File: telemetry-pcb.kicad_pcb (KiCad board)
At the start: 4 copper layers, 105 x 70 mm, 79 parts, among them CN1 12V, CN2 UART, CN3 RS232, CN5 THERMO1, CN6 THERMO2, CN8 GPS, IC1 MAX3232CPWR, IC2 MAX31855K, IC3 MAX31855K, IC4 MCP2515-xSO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

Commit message: routing update
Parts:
- moved R9 13.2 mm to (185.4, 99.8), turned to 90 degrees
- moved R7 9.97 mm to (186.5, 73.2), turned to -90 degrees
- moved T6 3.19 mm to (170.7, 79.1)
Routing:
- net /SPI Peripherals/CANL: track 13.1 -> 43.2 mm
- net /SPI Peripherals/CANH: track 62.5 -> 49.6 mm, vias 1 -> 0
- net Net-(S2-A): track 50.3 -> 38.8 mm, vias 3 -> 2
- net /MO: track 65.8 -> 71.3 mm, vias 1 -> 0
- net Net-(J3-Pin_2): track 5.96 -> 9.17 mm
- net /Serial Peripherals/TX_232: track 51.7 -> 53.7 mm
- net +3V3: track 52.8 -> 50.9 mm
- net /MI: track 82.0 -> 83.9 mm, vias 1 -> 2
- net /Serial Peripherals/RX_232: track 49.5 -> 51.0 mm
- net Net-(J2-Pin_5): track 70.0 -> 68.6 mm
- net /A1: track 83.4 -> 84.8 mm, vias 2 -> 1
- net /A0: track 71.7 -> 73.0 mm
- net /SCK: track 92.2 -> 93.5 mm
- net /SDA: track 131.5 -> 132.7 mm
- net Net-(IC1-ROUT1): track 79.8 -> 80.8 mm
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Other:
- outline, holes or cut-outs redrawn

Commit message: a
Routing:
- net GND: track 66.1 -> 67.8 mm, vias 29 -> 30
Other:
- outline, holes or cut-outs redrawn
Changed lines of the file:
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@@
 	)
 	(gr_line
-		(start 94.8944 54.682)
+		(start 94.9706 54.682)
 		(end 189.8396 54.686029)
 		(stroke
@@
 	)
 	(gr_arc
-		(start 194.945312 119.679866)
-		(mid 193.505286 123.184076)
-		(end 190.0174 124.6632)
+		(start 194.945511 119.679866)
+		(mid 193.505427 123.184216)
+		(end 190.017401 124.663399)
 		(stroke
 			(width 0.1)
@@
 	)
 	(gr_arc
-		(start 90 59.682)
-		(mid 91.464466 56.146466)
-		(end 95 54.682)
+		(start 89.999914 59.682)
+		(mid 91.454026 56.156815)
+		(end 94.9706 54.682)
 		(stroke
 			(width 0.1)
@@
 	)
 	(segment
+		(start 160.3248 100.4062)
+		(end 161.18 100.4062)
+		(width 0.25)
+		(layer "F.Cu")
+		(net 1)
+	)
+	(segment
 		(start 114.189 113.093)
 		(end 114.25 113.032)
@@
 	)
 	(segment
+		(start 161.18 100.4062)
+		(end 161.8018 101.028)
+		(width 0.25)
+		(layer "F.Cu")
+		(net 1)
+	)
+	(segment
 		(start 140.4607 84.6582)
 		(end 140.0134 85.1055)
@@
 		(zone_layer_connections "In1.Cu")
 		(net 1)
+	)
+	(via
+		(at 160.3248 100.4062)
+		(size 0.8)
+		(drill 0.4)
+		(layers "F.Cu" "B.Cu")
+		(remove_unused_layers yes)
+		(keep_end_layers no)
+		(free yes)
+		(zone_layer_connections "In1.Cu")
+		(net 1)

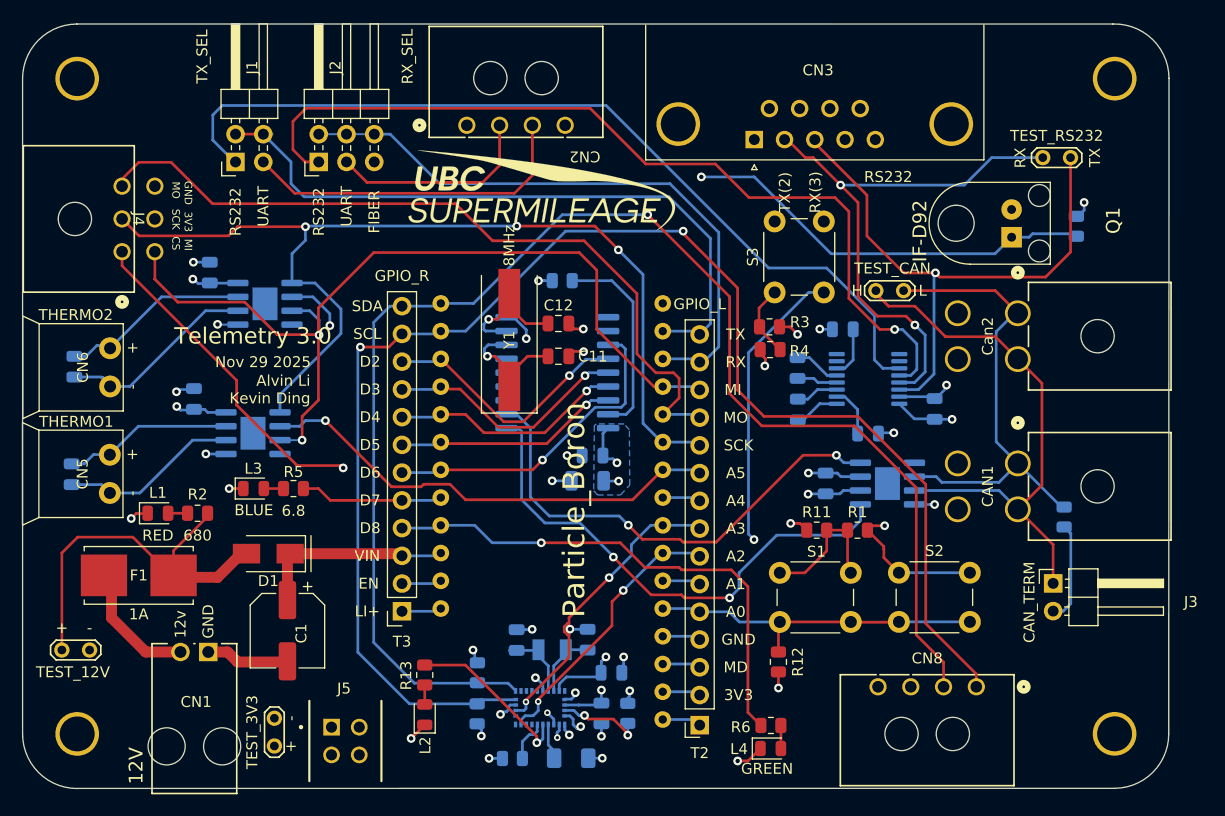
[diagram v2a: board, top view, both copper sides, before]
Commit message: connector changes
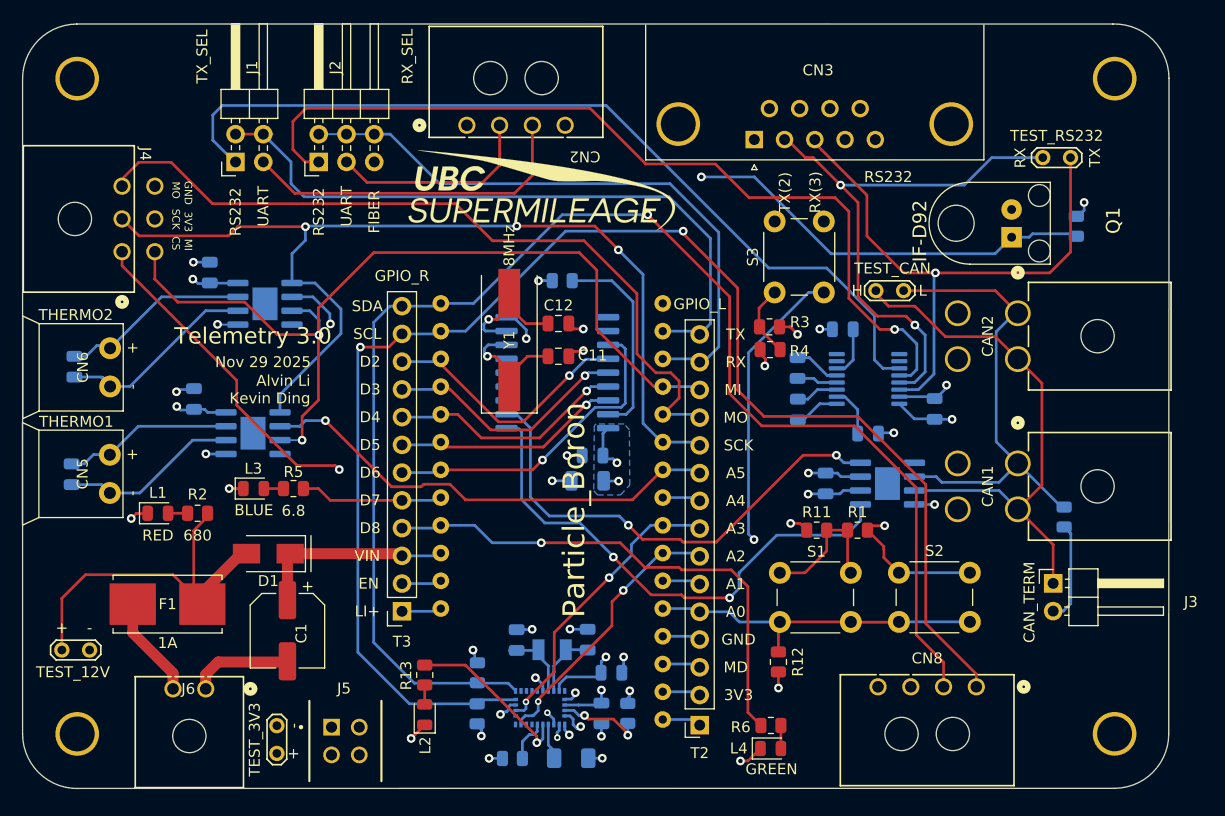
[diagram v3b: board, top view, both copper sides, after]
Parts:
- removed CN1: 12V, telemetry-pcb:molex_sl_1x02_horizontal
- added J6: 436500201, Footprints:CONN_SD-43650-001_02_MOL, F.Cu at (106.8, 115.6)
- moved F1 3.73 mm to (103.3, 107.8)
- moved T4 0.72 mm to (113.3, 121.5)
- renumbered Can2 to CAN2
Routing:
- net /A4: track 56.5 -> 53.4 mm
- net Net-(D1-A): track 33.8 -> 36.5 mm
- net GND: track 67.8 -> 69.4 mm
- net /A3: track 27.6 -> 27.1 mm

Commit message: more changes
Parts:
- R5: value 6.8 -> 150
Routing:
- net /A1: track 84.5 -> 81.7 mm
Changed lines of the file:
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@@
 		(tags "LED")
 		(property "Reference" "L3"
-			(at -0.0286 -1.8288 0)
+			(at -0.0794 -1.6378 0)
 			(layer "F.SilkS")
 			(effects
@@
 		(tags "resistor")
 		(property "Reference" "R5"
-			(at 0 1.524 0)
+			(at 0 1.587 0)
 			(layer "F.SilkS")
 			(effects
@@
 			)
 		)
-		(property "Value" "6.8"
-			(at 0 -2.032 0)
+		(property "Value" "150"
+			(at -0.0298 -1.9944 0)
 			(layer "F.SilkS")
 			(effects
@@
 		(tags "Through hole angled pin header THT 1x02 2.54mm single row")
 		(property "Reference" "J3"
-			(at 12.6084 1.6975 180)
+			(at 9.2862 1.2387 270)
 			(layer "F.SilkS")
 			(effects
@@
 		)
 		(fp_text user "${REFERENCE}"
-			(at 9.3634 1.4485 270)
+			(at 9.337 -1.0981 270)
 			(layer "F.Fab")
 			(effects
@@
 		)
 		(fp_text user "RX(3)"
-			(at -5.588 -4.826 90)
+			(at -5.5372 -4.1039 90)
 			(layer "F.SilkS")
 			(effects
@@
 		)
 		(fp_text user "TX(2)"
-			(at -2.794 -4.826 90)
+			(at -2.6416 -3.9515 90)
 			(layer "F.SilkS")
 			(effects
@@
 	)
 	(segment
-		(start 99.949 99.9612)
+		(start 100.0506 99.8596)
 		(end 100.4062 99.504)
 		(width 0.25)
@@
 	)
 	(segment
+		(start 100.4062 99.504)
+		(end 101.4245 99.504)
+		(width 0.25)
+		(layer "F.Cu")
+		(net 1)
+	)
+	(segment
 		(start 175.7384 80.1746)
 		(end 175.7384 80.128)
@@
 	)
 	(segment
-		(start 101.4245 99.504)
-		(end 101.4499 99.4786)
+		(start 100.0506 99.8728)
+		(end 100.0506 99.8596)
 		(width 0.25)
 		(layer "F.Cu")
@@
 	)
 	(segment
-		(start 100.4062 99.504)
-		(end 101.4245 99.504)
+		(start 101.4245 99.504)
+		(end 101.4499 99.4786)
 		(width 0.25)
 		(layer "F.Cu")
@@
 	)
 	(via
-		(at 99.949 99.9612)
+		(at 100.0506 99.8728)
 		(size 0.8)
 		(drill 0.4)
@@
 	)
 	(segment
+		(start 129.2347 94.5642)
+		(end 128.2954 95.5035)
+		(width 0.25)
+		(layer "F.Cu")
+		(net 9)
+	)
+	(segment
 		(start 137.60322 94.6055)
-		(end 136.70522 95.5035)
+		(end 137.56192 94.5642)
 		(width 0.25)
 		(layer "F.Cu")
@@
 	)
 	(segment
-		(start 136.70522 95.5035)
-		(end 128.2954 95.5035)
+		(start 137.56192 94.5642)
+		(end 129.2347 94.5642)
 		(width 0.25)
 		(layer "F.Cu")
@@
 	)
 	(segment
-		(start 148.5969 105.682)
-		(end 148.6154 105.6635)
-		(width 0.25)
-		(layer "F.Cu")
-		(net 13)
-	)
-	(segment
-		(start 115.1382 95.1098)
-		(end 109.601 89.5726)
+		(start 99.109701 76.820701)
+		(end 99.109701 75.529199)
 		(width 0.25)
 		(layer "F.Cu")
@@
 	)
 	(segment
-		(start 109.601 89.5726)
-		(end 109.601 87.312)
+		(start 109.601 87.312)
+		(end 99.109701 76.820701)
 		(width 0.25)
 		(layer "F.Cu")
@@
 	)
 	(segment
-		(start 118.999 95.4786)
-		(end 118.6302 95.1098)
+		(start 148.5969 105.682)
+		(end 148.6154 105.6635)
 		(width 0.25)
 		(layer "F.Cu")
@@
 	)
 	(segment
-		(start 118.6302 95.1098)
-		(end 115.1382 95.1098)
+		(start 109.601 88.519)
+		(end 109.601 87.312)
 		(width 0.25)
 		(layer "F.Cu")
@@
 	)
 	(segment
-		(start 109.601 87.312)
-		(end 99.109701 76.820701)
+		(start 116.967 95.1098)
+		(end 116.1918 95.1098)
 		(width 0.25)
 		(layer "F.Cu")
@@
 	)
 	(segment
-		(start 99.109701 76.820701)
-		(end 99.109701 75.529199)
+		(start 116.1918 95.1098)
+		(end 109.601 88.519)
 		(width 0.25)
 		(layer "F.Cu")
@@
 	)
 	(via
-		(at 118.999 95.4786)
+		(at 116.967 95.1098)
 		(size 0.8)
 		(drill 0.4)
@@
 	)
 	(segment
-		(start 142.7861 111.4928)
-		(end 148.6154 105.6635)
+		(start 137.6934 111.4928)
+		(end 142.7861 111.4928)
 		(width 0.25)
 		(layer "In2.Cu")
@@
 	)
 	(segment
-		(start 119.997 113.8116)
+		(start 119.3546 110.998)
+		(end 122.1682 113.8116)
+		(width 0.25)
+		(layer "In2.Cu")
+		(net 13)
+	)
+	(segment
+		(start 122.1682 113.8116)
 		(end 135.3746 113.8116)
 		(width 0.25)
@@
 	)
 	(segment
-		(start 119.3546 95.8342)
-		(end 119.3546 113.1692)
+		(start 116.9792 95.1098)
+		(end 119.3546 97.4852)
 		(width 0.25)
 		(layer "In2.Cu")
@@
 	)
 	(segment
-		(start 118.999 95.4786)
-		(end 119.3546 95.8342)
+		(start 116.967 95.1098)
+		(end 116.9792 95.1098)
 		(width 0.25)
 		(layer "In2.Cu")
@@
 	)
 	(segment
-		(start 119.3546 113.1692)
-		(end 119.997 113.8116)
+		(start 119.3546 97.4852)
+		(end 119.3546 110.998)
 		(width 0.25)
 		(layer "In2.Cu")
@@
 	)
 	(segment
-		(start 135.3746 113.8116)
-		(end 137.6934 111.4928)
+		(start 142.7861 111.4928)
+		(end 148.6154 105.6635)
 		(width 0.25)
 		(layer "In2.Cu")
@@
 	)
 	(segment
-		(start 137.6934 111.4928)
-		(end 142.7861 111.4928)
+		(start 135.3746 113.8116)
+		(end 137.6934 111.4928)
 		(width 0.25)
 		(layer "In2.Cu")
@@
 	)
 	(segment
-		(start 138.684 110.4006)
-		(end 138.684 114.0074)
+		(start 143.5262 105.5584)
+		(end 143.5262 109.1652)
 		(width 0.25)
 		(layer "F.Cu")
@@
 	)
 	(segment
-		(start 136.0932 116.5982)
-		(end 136.0932 116.7506)
+		(start 143.5262 109.1652)
+		(end 136.0932 116.5982)
 		(width 0.25)
 		(layer "F.Cu")
@@
 	)
 	(segment
-		(start 138.684 114.0074)
-		(end 136.0932 116.5982)
+		(start 136.0932 116.5982)
+		(end 136.0932 116.7506)
 		(width 0.25)
 		(layer "F.Cu")
@@
 	(segment
 		(start 143.7066 105.378)
-		(end 138.684 110.4006)
+		(end 143.5262 105.5584)
 		(width 0.25)
 		(layer "F.Cu")
@@
 	)
 	(segment
-		(start 117.094 83.121)
-		(end 113.3094 83.121)
-		(width 0.25)
-		(layer "F.Cu")
-		(net 23)
-	)
-	(segment
 		(start 142.5702 82.6516)
 		(end 142.5702 77.216)
@@
 	)
 	(segment
-		(start 102.1097 78.0393)
-		(end 102.1097 75.529199)
-		(width 0.25)
-		(layer "F.Cu")
-		(net 23)
-	)
-	(segment
-		(start 110.3376 80.1492)
-		(end 104.2162 80.1492)
+		(start 117.094 83.121)
+		(end 107.188 83.121)
 		(width 0.25)
 		(layer "F.Cu")
@@
 	)
 	(segment
-		(start 113.3094 83.121)
-		(end 110.3376 80.1492)
+		(start 107.188 83.121)
+		(end 102.108 78.041)
 		(width 0.25)
 		(layer "F.Cu")
@@
 	)
 	(segment
-		(start 104.2162 80.1492)
-		(end 102.108 78.041)
+		(start 148.6154 87.8835)
+		(end 147.8021 87.8835)
 		(width 0.25)
 		(layer "F.Cu")
@@
 	)
 	(segment
-		(start 148.6154 87.8835)
-		(end 147.8021 87.8835)
+		(start 102.1097 78.0393)
+		(end 102.1097 75.529199)
 		(width 0.25)
 		(layer "F.Cu")
@@
 	)
 	(segment
-		(start 150.114 88.9249)
-		(end 148.6154 90.4235)
+		(start 147.98371 86.614)
+		(end 149.352 86.614)
 		(width 0.25)
 		(layer "F.Cu")
@@
 	)
 	(segment
-		(start 129.6416 71.1322)
-		(end 133.0391 74.5297)
+		(start 150.114 88.9249)
+		(end 148.6154 90.4235)
 		(width 0.25)
 		(layer "F.Cu")
@@
 	)
 	(segment
-		(start 103.6066 67.3476)
-		(end 107.3912 71.1322)
+		(start 99.109701 69.529201)
+		(end 99.109701 68.872699)
 		(width 0.25)
 		(layer "F.Cu")
@@
 	)
 	(segment
-		(start 99.109701 68.872699)
-		(end 100.6348 67.3476)
+		(start 104.1532 67.8942)
+		(end 107.3912 71.1322)
 		(width 0.25)
 		(layer "F.Cu")
@@
 	)
 	(segment
-		(start 146.2532 84.88349)
-		(end 147.98371 86.614)
+		(start 129.6416 71.1322)
+		(end 133.0391 74.5297)
 		(width 0.25)
 		(layer "F.Cu")
@@
 	)
 	(segment
-		(start 141.4079 74.5297)
-		(end 146.2532 79.375)
+		(start 146.2532 84.88349)
+		(end 147.98371 86.614)
 		(width 0.25)
 		(layer "F.Cu")
@@
 	)
 	(segment
-		(start 150.114 87.376)
-		(end 150.114 88.9249)
+		(start 149.352 86.614)
+		(end 150.114 87.376)
 		(width 0.25)
 		(layer "F.Cu")
@@
 	)
 	(segment
-		(start 107.3912 71.1322)
-		(end 129.6416 71.1322)
+		(start 100.0882 67.8942)
+		(end 104.1532 67.8942)
 		(width 0.25)
 		(layer "F.Cu")
@@
 	)
 	(segment
-		(start 149.352 86.614)
-		(end 150.114 87.376)
+		(start 148.6154 90.5666)
+		(end 148.6154 90.4235)
 		(width 0.25)
 		(layer "F.Cu")
@@
 	)
 	(segment
-		(start 147.98371 86.614)
-		(end 149.352 86.614)
+		(start 99.109701 68.872699)
+		(end 100.0882 67.8942)
 		(width 0.25)
 		(layer "F.Cu")
@@
 	)
 	(segment
-		(start 100.6348 67.3476)
-		(end 103.6066 67.3476)
+		(start 146.2532 79.375)
+		(end 146.2532 84.88349)
 		(width 0.25)
 		(layer "F.Cu")
@@
 	)
 	(segment
-		(start 148.6154 90.5666)
-		(end 148.6154 90.4235)
+		(start 133.0391 74.5297)
+		(end 141.4079 74.5297)
 		(width 0.25)
 		(layer "F.Cu")
@@
 	)
 	(segment
-		(start 133.0391 74.5297)
-		(end 141.4079 74.5297)
+		(start 107.3912 71.1322)
+		(end 129.6416 71.1322)
 		(width 0.25)
 		(layer "F.Cu")
@@
 	)
 	(segment
-		(start 146.2532 79.375)
-		(end 146.2532 84.88349)
+		(start 141.4079 74.5297)
+		(end 146.2532 79.375)
 		(width 0.25)
 		(layer "F.Cu")
@@
 	)
 	(segment
-		(start 99.109701 69.529201)
-		(end 99.109701 68.872699)
+		(start 150.114 87.376)
+		(end 150.114 88.9249)
 		(width 0.25)
 		(layer "F.Cu")

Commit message: more changes
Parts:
- moved CN2 0.34 mm to (130.7, 63.6)
- moved CN8 0.32 mm to (177.3, 115.7)
- moved J6 0.22 mm to (106.7, 115.8)
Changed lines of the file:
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@@
 		(at 183.0984 72.9335 -90)
 		(property "Reference" "Q1"
-			(at 0.9805 -6.03 90)
+			(at 1.2853 -1.7882 90)
 			(layer "F.SilkS")
 			(effects
@@
 	(footprint "Footprints:CONN_SD-43650-001_04_MOL"
 		(layer "F.Cu")
-		(at 177.327999 115.368401)
+		(at 177.327999 115.686401)
 		(tags "436500400 ")
 		(property "Reference" "CN8"
@@
 	(footprint "Footprints:CONN_SD-43650-001_02_MOL"
 		(layer "F.Cu")
-		(at 106.7689 115.5573)
+		(at 106.7308 115.7732)
 		(property "Reference" "J6"
-			(at -1.6002 0 0)
+			(at -1.5113 -2.1463 0)
 			(layer "F.SilkS")
 			(effects
@@
 	(footprint "Footprints:CONN_SD-43650-001_04_MOL"
 		(layer "F.Cu")
-		(at 130.678801 63.9546 180)
+		(at 130.678801 63.6122 180)
 		(tags "436500400 ")
 		(property "Reference" "CN2"
@@
 		(tags "BNO055 ")
 		(property "Reference" "U1"
-			(at 0 0 0)
+			(at 2.032 2.476 0)
 			(unlocked yes)
 			(layer "B.SilkS")
@@
 	)
 	(segment
-		(start 106.7689 114.2351)
-		(end 107.911 113.093)
+		(start 106.7689 115.7351)
+		(end 106.7689 114.2351)
+		(width 1)
+		(layer "F.Cu")
+		(net 1)
+	)
+	(segment
+		(start 106.5657 115.5573)
+		(end 106.5657 115.6081)
 		(width 1)
 		(layer "F.Cu")
@@
 	)
 	(segment
-		(start 175.7384 80.1746)
-		(end 175.7384 80.128)
-		(width 0.25)
+		(start 107.911 113.093)
+		(end 114.189 113.093)
+		(width 1)
 		(layer "F.Cu")
 		(net 1)
@@
 	)
 	(segment
-		(start 156.4178 122.1608)
-		(end 157.5608 121.0178)
+		(start 175.7384 80.1746)
+		(end 175.7384 80.128)
 		(width 0.25)
 		(layer "F.Cu")
@@
 	)
 	(segment
-		(start 106.5657 115.5573)
-		(end 106.7689 115.5573)
-		(width 1)
+		(start 156.4178 122.1608)
+		(end 157.5608 121.0178)
+		(width 0.25)
 		(layer "F.Cu")
 		(net 1)
@@
 	)
 	(segment
+		(start 106.5657 115.6081)
+		(end 106.7308 115.7732)
+		(width 1)
+		(layer "F.Cu")
+		(net 1)
+	)
+	(segment
+		(start 106.7689 114.2351)
+		(end 107.911 113.093)
+		(width 1)
+		(layer "F.Cu")
+		(net 1)
+	)
+	(segment
 		(start 100.0506 99.8728)
 		(end 100.0506 99.8596)
@@
 	)
 	(segment
-		(start 141.343288 82.6055)
-		(end 140.5134 82.6055)
-		(width 0.25)
+		(start 106.7308 115.7732)
+		(end 106.7689 115.7351)
+		(width 1)
 		(layer "F.Cu")
 		(net 1)
 	)
 	(segment
-		(start 107.911 113.093)
-		(end 114.189 113.093)
-		(width 1)
+		(start 141.343288 82.6055)
+		(end 140.5134 82.6055)
+		(width 0.25)
 		(layer "F.Cu")
 		(net 1)
@@
 		(net 1)
 	)
-	(segment
-		(start 106.7689 115.5573)
-		(end 106.7689 114.2351)
-		(width 1)
-		(layer "F.Cu")
-		(net 1)
-	)
 	(via
 		(at 106.7816 94.043)
@@
 	)
 	(segment
-		(start 155.4734 88.201)
-		(end 155.4734 78.8555)
+		(start 150.4884 73.8705)
+		(end 150.4884 73.6468)
 		(width 0.25)
 		(layer "F.Cu")
@@
 	)
 	(segment
-		(start 157.8864 90.614)
-		(end 155.4734 88.201)
+		(start 166.4716 90.614)
+		(end 157.8864 90.614)
 		(width 0.25)
 		(layer "F.Cu")
@@
 	)
 	(segment
-		(start 172.6946 109.5756)
-		(end 172.6946 96.837)
+		(start 155.4734 78.8555)
+		(end 150.4884 73.8705)
 		(width 0.25)
 		(layer "F.Cu")
@@
 	)
 	(segment
-		(start 172.6946 96.837)
-		(end 166.4716 90.614)
+		(start 172.6946 109.5756)
+		(end 172.6946 96.837)
 		(width 0.25)
 		(layer "F.Cu")
@@
 	)
 	(segment
-		(start 177.327999 115.368401)
-		(end 177.327999 114.208999)
+		(start 155.4734 88.201)
+		(end 155.4734 78.8555)
 		(width 0.25)
 		(layer "F.Cu")
@@
 	)
 	(segment
-		(start 120.9294 84.264)
-		(end 123.5329 84.264)
+		(start 157.8864 90.614)
+		(end 155.4734 88.201)
 		(width 0.25)
 		(layer "F.Cu")
@@
 	)
 	(segment
-		(start 150.4884 73.8705)
-		(end 150.4884 73.6468)
+		(start 120.9294 84.264)
+		(end 123.5329 84.264)
 		(width 0.25)
 		(layer "F.Cu")
@@
 	)
 	(segment
-		(start 155.4734 78.8555)
-		(end 150.4884 73.8705)
+		(start 177.327999 114.208999)
+		(end 172.6946 109.5756)
 		(width 0.25)
 		(layer "F.Cu")
@@
 	)
 	(segment
-		(start 166.4716 90.614)
-		(end 157.8864 90.614)
+		(start 123.5329 84.264)
+		(end 124.7394 83.0575)
 		(width 0.25)
 		(layer "F.Cu")
@@
 	)
 	(segment
-		(start 123.5329 84.264)
-		(end 124.7394 83.0575)
+		(start 177.327999 115.368401)
+		(end 177.327999 114.208999)
 		(width 0.25)
 		(layer "F.Cu")
@@
 	)
 	(segment
-		(start 177.327999 114.208999)
-		(end 172.6946 109.5756)
+		(start 172.6946 96.837)
+		(end 166.4716 90.614)
 		(width 0.25)
 		(layer "F.Cu")
@@
 	)
 	(segment
-		(start 171.831 110.617)
-		(end 171.831 97.1418)
+		(start 154.7384 88.5328)
+		(end 154.7384 79.6482)
 		(width 0.25)
 		(layer "F.Cu")
@@
 	)
 	(segment
-		(start 154.7384 79.6482)
-		(end 147.2384 72.1482)
+		(start 166.1668 91.4776)
+		(end 157.6832 91.4776)
 		(width 0.25)
 		(layer "F.Cu")
@@
 	)
 	(segment
-		(start 171.831 97.1418)
-		(end 166.1668 91.4776)
+		(start 174.328 115.368401)
+		(end 174.328 113.114)
 		(width 0.25)
 		(layer "F.Cu")
@@
 	)
 	(segment
-		(start 154.7384 88.5328)
-		(end 154.7384 79.6482)
+		(start 157.6832 91.4776)
+		(end 154.7384 88.5328)
 		(width 0.25)
 		(layer "F.Cu")
@@
 	)
 	(segment
-		(start 174.328 113.114)
-		(end 171.831 110.617)
+		(start 171.831 97.1418)
+		(end 166.1668 91.4776)
 		(width 0.25)
 		(layer "F.Cu")
@@
 	)
 	(segment
-		(start 166.1668 91.4776)
-		(end 157.6832 91.4776)
+		(start 174.328 113.114)
+		(end 171.831 110.617)
 		(width 0.25)
 		(layer "F.Cu")
@@
 	)
 	(segment
-		(start 157.6832 91.4776)
-		(end 154.7384 88.5328)
+		(start 154.7384 79.6482)
+		(end 147.2384 72.1482)
 		(width 0.25)
 		(layer "F.Cu")
@@
 	)
 	(segment
-		(start 174.328 115.368401)
-		(end 174.328 113.114)
+		(start 171.831 110.617)
+		(end 171.831 97.1418)
 		(width 0.25)
 		(layer "F.Cu")
@@
 	)
 	(segment
-		(start 114.9119 70.182)
-		(end 135.0368 70.182)
+		(start 136.678799 63.9546)
+		(end 136.678799 68.540001)
 		(width 0.25)
 		(layer "F.Cu")
@@
 	)
 	(segment
-		(start 112.0394 67.3095)
+		(start 135.0368 70.182)
 		(end 114.9119 70.182)
 		(width 0.25)
@@
 	)
 	(segment
-		(start 136.678799 63.9546)
-		(end 136.678799 68.540001)
+		(start 114.9119 70.182)
+		(end 112.0394 67.3095)
 		(width 0.25)
 		(layer "F.Cu")
@@
 	(segment
 		(start 136.678799 68.540001)
-		(end 136.4107 68.8081)
-		(width 0.25)
-		(layer "F.Cu")
-		(net 72)
-	)
-	(segment
-		(start 135.0368 70.182)
-		(end 136.4107 68.8081)
+		(end 135.0368 70.182)
 		(width 0.25)
 		(layer "F.Cu")
@@
 	)
 	(segment
-		(start 121.5319 69.182)
-		(end 119.6594 67.3095)
+		(start 133.6788 67.6284)
+		(end 132.1252 69.182)
 		(width 0.25)
 		(layer "F.Cu")
@@
 	)
 	(segment
-		(start 133.6788 63.9546)
-		(end 133.6788 67.6284)
+		(start 121.5319 69.182)
+		(end 119.6594 67.3095)
 		(width 0.25)
 		(layer "F.Cu")
@@
 	)
 	(segment
-		(start 133.6788 67.6284)
-		(end 132.1252 69.182)
+		(start 133.6788 63.6122)
+		(end 133.6788 67.6284)
 		(width 0.25)
 		(layer "F.Cu")
@@
 	)
 	(segment
-		(start 103.7717 114.1095)
-		(end 103.7717 115.5573)
+		(start 103.5685 115.6081)
+		(end 103.5685 115.5573)
+		(width 1)
+		(layer "F.Cu")
+		(net 95)
+	)
+	(segment
+		(start 103.7336 115.7732)
+		(end 103.5685 115.6081)
 		(width 1)
 		(layer "F.Cu")
@@
 	)
 	(segment
-		(start 100.0887 107.7976)
-		(end 100.0887 110.4265)
+		(start 103.7717 115.7351)
+		(end 103.7336 115.7732)
 		(width 1)
 		(layer "F.Cu")
@@
 	)
 	(segment
-		(start 103.7717 115.5573)
-		(end 103.5685 115.5573)
+		(start 103.7717 114.1095)
+		(end 103.7717 115.7351)
+		(width 1)
+		(layer "F.Cu")
+		(net 95)
+	)
+	(segment
+		(start 100.0887 107.7976)
+		(end 100.0887 110.4265)
 		(width 1)
 		(layer "F.Cu")
